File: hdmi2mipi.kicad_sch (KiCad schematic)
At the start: 154 parts, among them J1 AudioJack3, J10 BOOT, J11 USB_C_Receptacle_USB2.0, J2 HDMI_A_1.4, J4 TP, J5 QWIIC, J7 SWD, J9 QWIIC, Q1 BC846, Q2 BC846, Q3 BC846, Q4 BC846, Q5 BC846, Q6 BC846, Q7 2SC2712, U1 MS4344, U1 RP2040, U2 W25Q16JVUXIQ, U3 SY6280AAC, U3 W25Q16JVUXIQ, U4 PCA9306DC, U4 SY8079AAC, X2 SG-210STF, Y1 12MHz

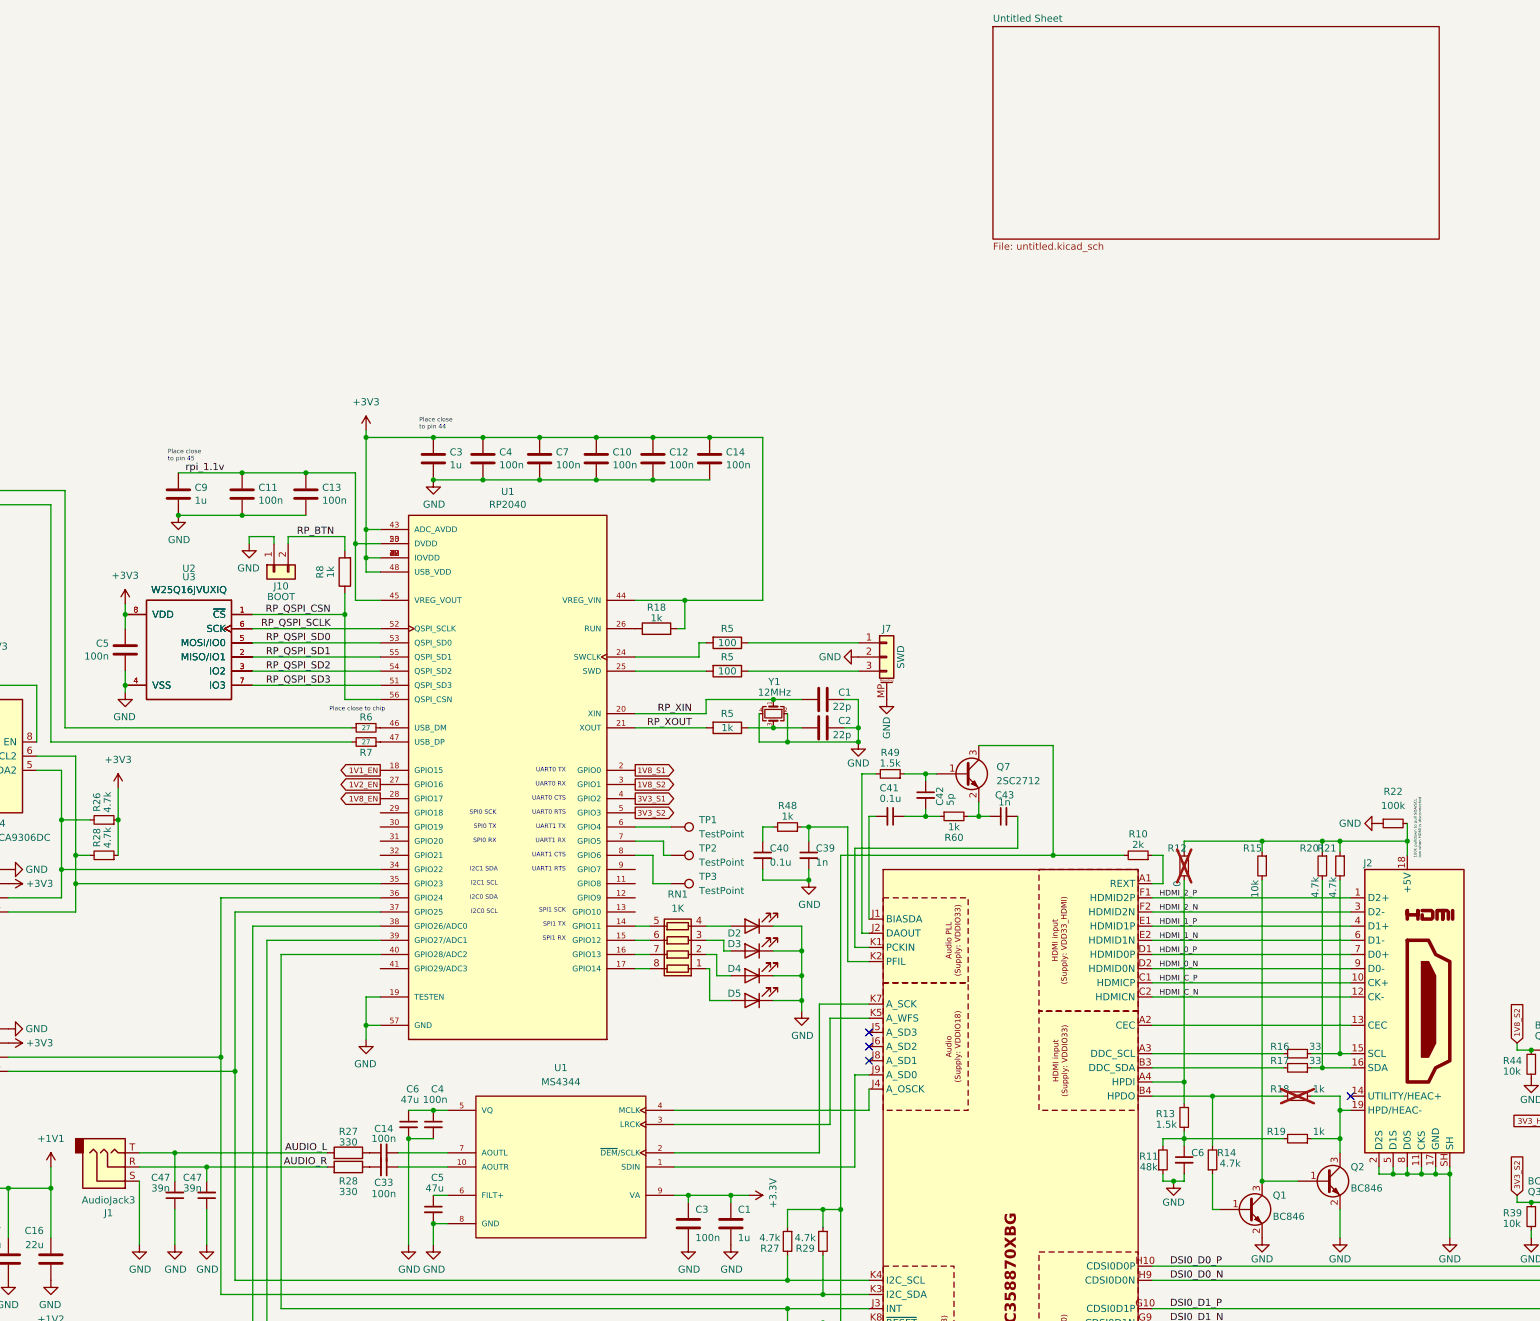
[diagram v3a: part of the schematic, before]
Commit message: Fix board outline and center circuit board on grid
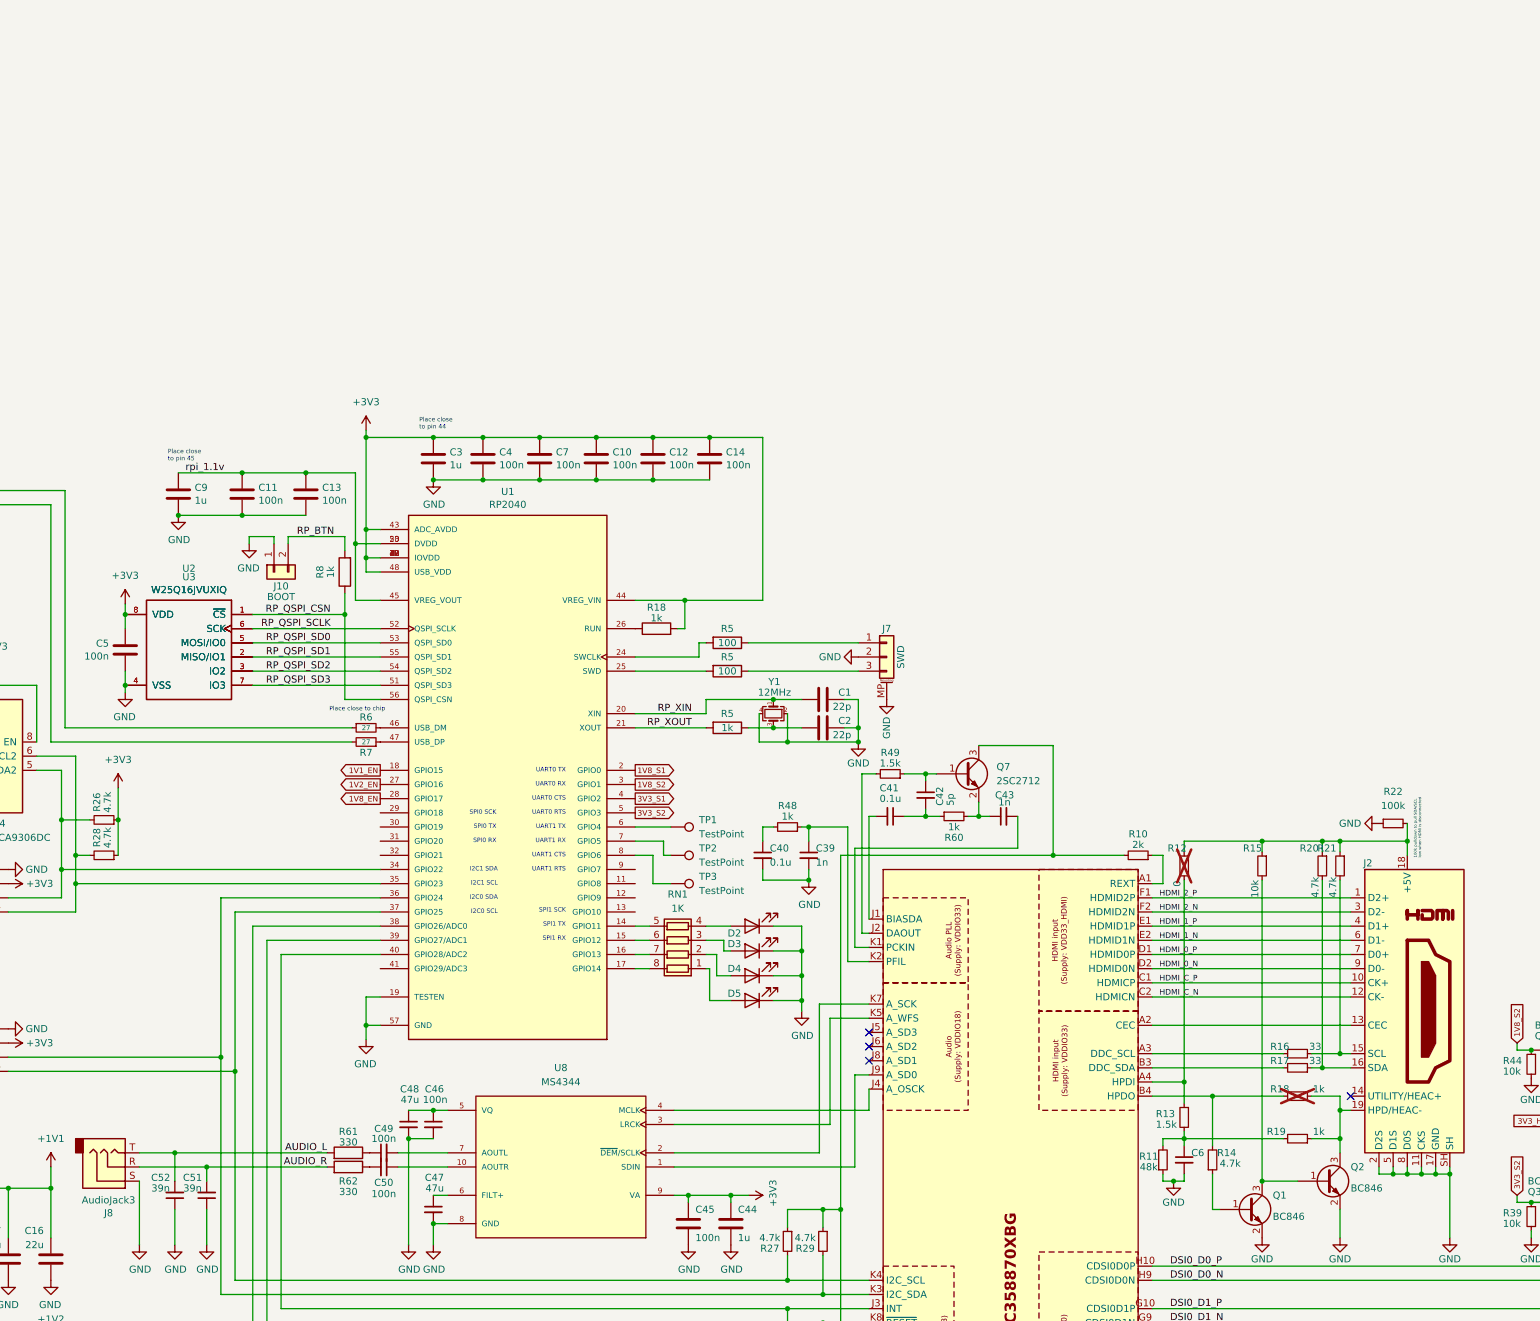
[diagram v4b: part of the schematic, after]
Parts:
- renumbered C1 to C44, C3 to C45, C4 to C46, C5 to C47, C6 to C48, C14 to C49, C33 to C50, C47 to C51, C47 to C52, J1 to J8, R27 to R61, R28 to R62, U1 to U8
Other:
- removed sheet Untitled Sheet

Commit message: Backlight driver
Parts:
- added C53: 2.2u, Capacitor_SMD:C_0402_1005Metric, symbol Device:C_Small
- added C54: ~, Capacitor_SMD:C_0402_1005Metric, symbol Device:C_Small
- added D5: D, symbol Device:D
- added L5: ~, symbol mch2021-rescue:L-Device
- added R1: 10k, Resistor_SMD:R_0402_1005Metric, symbol Device:R_Small
- added R2: 0, Resistor_SMD:R_0402_1005Metric, symbol mch2021-rescue:R-Device
- added R3, R4: 10, Resistor_SMD:R_0402_1005Metric, symbol mch2021-rescue:R-Device
- added R5: 6.8k, Resistor_SMD:R_0402_1005Metric, symbol mch2021-rescue:R-Device
- added R63: 50k, Resistor_SMD:R_0402_1005Metric, symbol mch2021-rescue:R-Device
- added R64: 100k, Resistor_SMD:R_0402_1005Metric, symbol mch2021-rescue:R-Device
- added TP4, TP5: TestPoint, TestPoint:TestPoint_Pad_D2.0mm, symbol Connector:TestPoint
- added U12: ~, Package_TO_SOT_SMD:SOT-23-6, symbol lp3382s:LP3382S
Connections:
- net GND: now also C53.2, C54.2, R1.2, R2.1, U12.2 (GND)
- net VBUS: now also L5.2, U12.6 (Vin)
- net at J3.1 (FB1), J3.2 (FB1): now also R2.2, R3.1, R4.1
- net at J3.10 (LED+), J3.8 (LED+), J3.9 (LED+): now also C53.1, D5.1 (K), U12.5 (OVP)
- net at J3.13 (5.8v-VEE): now also TP4.1
- net at J3.14 (5.8v-VDD): now also TP5.1
- net at J3.27 (3.3-S2), Q3.3 (C), R41.2: now also J3.28 (3.3-S1), Q4.3 (C), R43.2
- net at J3.5 (FB2), J3.6 (FB2): now also R3.2, R4.2, R5.1
- net BL_EN: now reaches U1.29 (GPIO18)
- net BL_EN: now also R1.1, U12.4 (EN)
- net BL_PWM: now reaches U1.30 (GPIO19)
- net BL_PWM: now also R64.2
- new net: R5.2, R63.1, U12.3 (FB)
- new net: D5.2 (A), L5.1, U12.1 (LX)
- new net: C54.1, R63.2, R64.1
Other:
- note removed: "No clue yet how these are supposed to work"
- moved on the sheet: C1, C10, C11, C12, C13, C14, C15, C16, C17, C2, C3, C39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

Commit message: Fill more BOM entries
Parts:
- C1, C15, C2: Buy early Y -> (none); Category Capacitors -> (none); MANUFACTURER YAGEO -> (none); MPN TCC0402C0G220J500AT -> (none); Manufacturer CCTC -> (none); Minimal voltage rating 10 -> (none); Sponsored N -> (none); Voltage rating 50 -> (none)
- C10, C11, C12, C13, C14, C4, C5, C7: Buy early Y -> (none); Category Capacitors -> (none); MPN CL05B104KB54PNC -> (none); Manufacturer Samsung Electro-Mechanics -> (none); Minimal voltage rating 10 -> (none); Mouser - -> (none); Sponsored N -> (none); Voltage rating 50 -> (none)
- C16, C17, C8: Buy early Y -> (none); Category Capacitors -> (none); MPN CL21A226MAYNNNE -> (none); Manufacturer Samsung Electro-Mechanics -> (none); Minimal voltage rating 10 -> (none); Sponsored N -> (none); Voltage rating 25 -> (none)
- C3, C9: Buy early Y -> (none); Category Capacitors -> (none); MPN CL05A105KQ5NNNC -> (none); Manufacturer Samsung Electro-Mechanics -> (none); Minimal voltage rating 6 -> (none); Mouser - -> (none); Sponsored N -> (none); Voltage rating 6.3 -> (none)
- C44: Buy early Y -> (none); Category Capacitors -> (none); MPN CL05A105KQ5NNNC -> (none); Manufacturer Samsung Electro-Mechanics -> (none); Minimal voltage rating 6 -> (none); Sponsored N -> (none); Voltage rating 6.3 -> (none)
- C45, C46, C49, C50, C6: Buy early Y -> (none); Category Capacitors -> (none); MPN CL05B104KB54PNC -> (none); Manufacturer Samsung Electro-Mechanics -> (none); Minimal voltage rating 10 -> (none); Sponsored N -> (none); Voltage rating 50 -> (none)
- C47, C48: Buy early Y -> (none); Category Capacitors -> (none); MPN CL21A476MQYNNNE -> (none); Manufacturer Samsung Electro-Mechanics -> (none); Minimal voltage rating 6 -> (none); Sponsored N -> (none); Voltage rating 6.3 -> (none)
- C51, C52: Buy early Y -> (none); Category Capacitors -> (none); MPN TCC0402X7R393K500AT -> (none); Manufacturer CCTC -> (none); Minimal voltage rating 10 -> (none); Sponsored N -> (none); Voltage rating 50 -> (none)
- J11: LCSC (none) -> C165948
- J4: value TP -> TOUCH
- J8: Buy early Y -> (none); Category Connectors -> (none); MPN C18594 -> (none); Manufacturer Boomele -> (none); Mouser - -> (none); Sponsored N -> (none)
- L1: Buy early Y -> (none); Category Inductors -> (none); MPN MCS20FC-2R2MHC -> (none); Manufacturer PSA -> (none); Mouser - -> (none); Sponsored N -> (none)
- R1, R15, R17, R38, R39, R40, R42, R44, R46, R50: LCSC (none) -> C25744
- R14, R15: Buy early Y -> (none); Category Resistors -> (none); LCSC (none) -> C25941; MANUFACTURER UNI-ROYAL -> (none); Manufacturer Uni-royal -> (none); Mouser - -> (none); Sponsored N -> (none)
- R14, R20, R21, R23, R24, R25, R26, R27, R28, R29, R41, R43, R45, R47: LCSC (none) -> C25900
- R16, R17, R37: LCSC (none) -> C25105
- R16: Buy early Y -> (none); Category Resistors -> (none); MANUFACTURER UNI-ROYAL -> (none); MPN 0402WGF1002TCE -> (none); Manufacturer Uni-royal -> (none); Mouser - -> (none); Sponsored N -> (none)
- R17: LCSC (none) -> C25545
- R17: Buy early Y -> (none); Category Resistors -> (none); MANUFACTURER UNI-ROYAL -> (none); MPN 0402WGF4532TCE -> (none); Manufacturer Uni-royal -> (none); Mouser - -> (none); Sponsored N -> (none)
- R17: LCSC (none) -> C26980
- R18, R5, R8: Buy early Y -> (none); Category Resistors -> (none); MANUFACTURER UNI-ROYAL -> (none); MPN 0402WGF1001TCE -> (none); Manufacturer Uni-royal -> (none); Mouser - -> (none); Sponsored N -> (none)
- R18, R19, R48, R60: LCSC (none) -> C11702
- R22, R64: LCSC (none) -> C25530
- R5: LCSC (none) -> C25138
- R6, R7: Buy early Y -> (none); Category Resistors -> (none); MANUFACTURER UNI-ROYAL -> (none); MPN 0402WGF270JTCE -> (none); Manufacturer Uni-royal -> (none); Mouser - -> (none); Sponsored N -> (none)
- R61, R62: Buy early Y -> (none); Category Resistors -> (none); MANUFACTURER UNI-ROYAL -> (none); MPN 0402WGD3300TCE -> (none); Manufacturer Uni-royal -> (none); Mouser - -> (none); Sponsored N -> (none)
- R63: value 50k -> 47k; LCSC (none) -> C25563
- RN1: LCSC (none) -> C25726
- U1: Buy early N -> (none); Category ICs -> (none); MANUFACTURER Raspberry Pi -> (none); MAXIMUM_PACKAGE_HEIGHT 0.9 mm -> (none); MPN RP2040 -> (none); Manufacturer Raspberry Pi -> (none); PARTREV 1.6.1 -> (none); STANDARD IPC 7351B -> (none); Sponsored Y -> (none)
- U2, U3: Buy early N -> (none); Category ICs -> (none); MPN W25Q16JVUXIQ -> (none); Manufacturer Winbond Elec -> (none); Sponsored Y -> (none)
- U4: Buy early Y -> (none); Category ICs -> (none); MPN SY8079AAC -> (none); Manufacturer Silergy Corp -> (none); Mouser - -> (none); Sponsored N -> (none)
- U8: Buy early Y -> (none); Category ICs -> (none); MPN MS4344 -> (none); Manufacturer Hangzhou Ruimeng Tech -> (none); Sponsored N -> (none)
- X2: Buy early Y -> (none); Category Oscillators -> (none); MPN SG-210STF 12.0000ML0 -> (none); Manufacturer Seiko Epson -> (none); Sponsored N -> (none)
- Y1: Buy early Y -> (none); Category Oscillators -> (none); MPN S3212000181080 -> (none); Manufacturer JGHC -> (none); Mouser - -> (none); Sponsored N -> (none)
